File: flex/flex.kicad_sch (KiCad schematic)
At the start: 71 parts, among them J1 NA_Conn_01x04_Female, J2 NA_Conn_01x05_Female, J3 NA_Conn_01x03_Female, J4 NA_Conn_01x06_Female, J5 NA_Conn_01x03_Female, SW10 NA_SW_Push, SW11 NA_SW_Push, SW12 NA_SW_Push, SW15 NA_SW_Push, SW16 NA_SW_Push, SW17 NA_SW_Push, SW20 NA_SW_Push, SW21 NA_SW_Push, SW22 NA_SW_Push, SW24 NA_SW_Push, SW25 NA_SW_Push, SW26 NA_SW_Push, SW6 NA_SW_Push, SW7 NA_SW_Push, SW8 NA_SW_Push

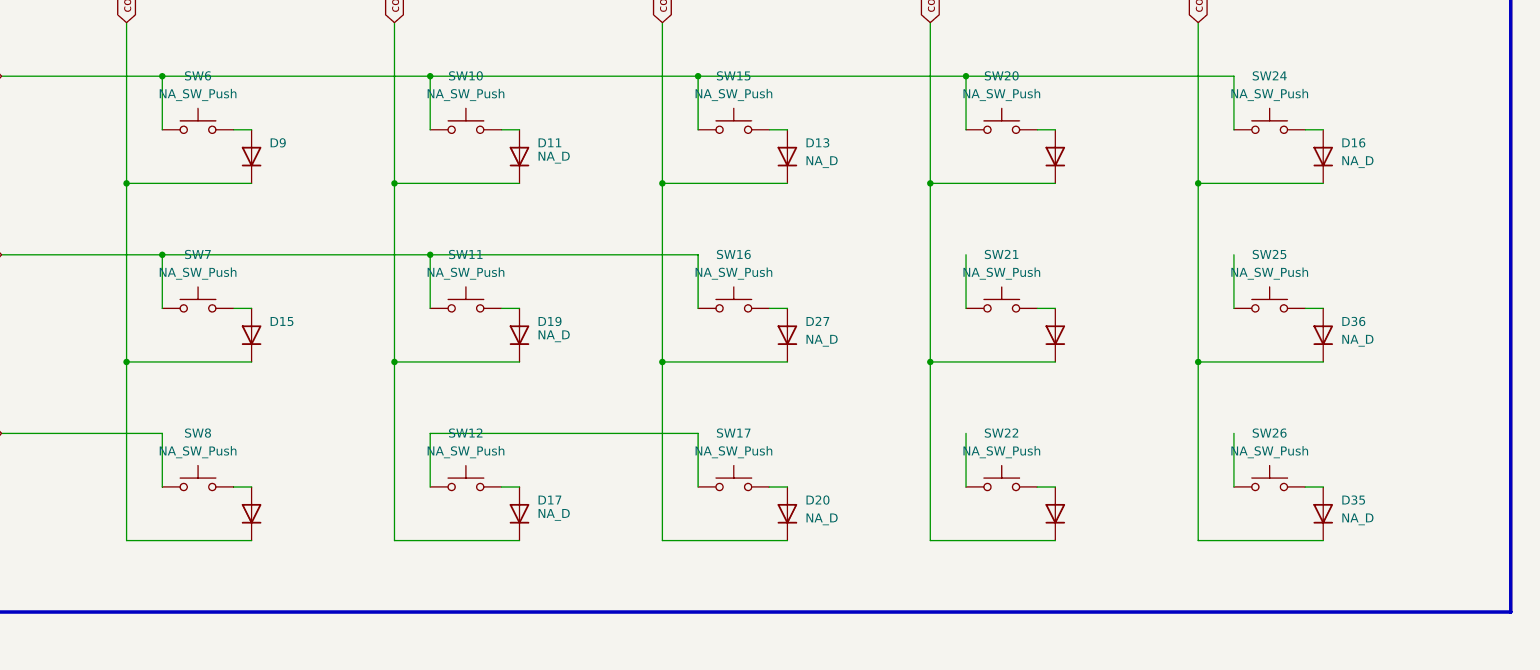
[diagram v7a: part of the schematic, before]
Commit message: update diode footprints
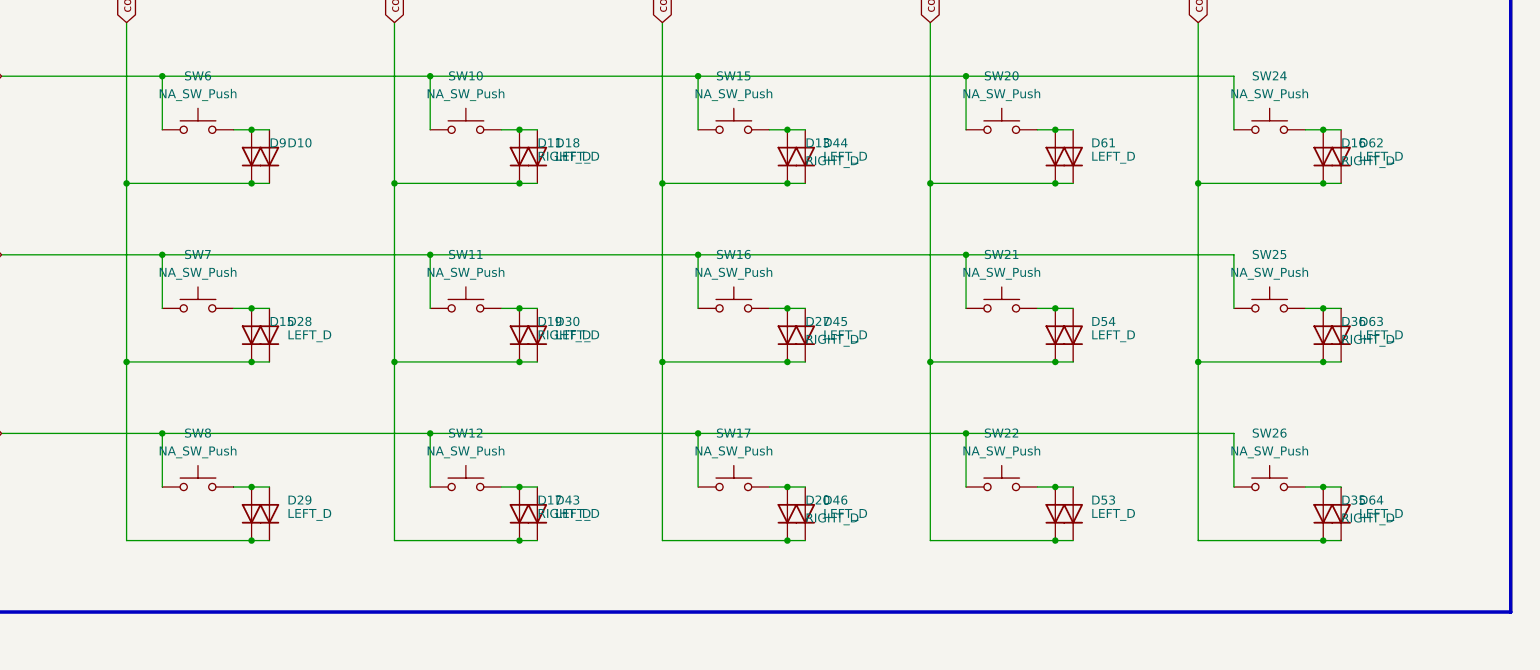
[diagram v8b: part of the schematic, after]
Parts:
- added D10, D18, D28, D29, D30, D43, D44, D45, D46, D53, D54, D61, D62, D63, D64: LEFT_D, customs:SOD123_assembly, symbol Device:D
- D11, D12, D13, D14, D15, D16, D17, D19, D20, D27, D31, D32, D35, D36, D9: value NA_D -> RIGHT_D; footprint custom:Diode_TH_SOD123 -> customs:SOD123_assembly
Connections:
- net col2: now also D10.1 (K), D28.1 (K), D29.1 (K)
- net col3: now also D18.1 (K), D30.1 (K), D43.1 (K)
- net col4: now also D44.1 (K), D45.1 (K), D46.1 (K)
- net col5: now also D53.1 (K), D54.1 (K), D61.1 (K)
- net col6: now also D62.1 (K), D63.1 (K), D64.1 (K)
- net row3: now also SW21.1, SW25.1
- net row4: now also SW12.1, SW17.1, SW22.1, SW26.1
- net at D27.2 (A), SW16.2: now also D45.2 (A)
- net at D9.2 (A), SW6.2: now also D10.2 (A)
- net at D17.2 (A), SW12.2: now also D43.2 (A)
- net at D31.2 (A), SW22.2: now also D53.2 (A)
- net at D32.2 (A), SW21.2: now also D54.2 (A)
- net at D35.2 (A), SW26.2: now also D64.2 (A)
- net at D19.2 (A), SW11.2: now also D30.2 (A)
- net at D20.2 (A), SW17.2: now also D46.2 (A)
- net at D12.2 (A), SW8.2: now also D29.2 (A)
- net at D16.2 (A), SW24.2: now also D62.2 (A)
- net at D14.2 (A), SW20.2: now also D61.2 (A)
- net at D36.2 (A), SW25.2: now also D63.2 (A)
- net at D11.2 (A), SW10.2: now also D18.2 (A)
- net at D13.2 (A), SW15.2: now also D44.2 (A)
- net at D15.2 (A), SW7.2: now also D28.2 (A)
